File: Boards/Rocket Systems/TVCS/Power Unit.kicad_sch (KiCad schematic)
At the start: 111 parts, among them IC3 CYPD3177-24LQXQT, IC8 DMP2040USD-13, IC9 DMP2040USD-13, J10 DX07S016JA1R1500, U13 LM61460AASQRJRRQ1, U14 LM61460AASQRJRRQ1, U4 LM61460AASQRJRRQ1

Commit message: TVCS fixes and required additions
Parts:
- added TP1, TP2, TP3: TestPoint, TestPoint:TestPoint_Pad_2.0x2.0mm, symbol Connector:TestPoint
- Rsense3: value 7.5m -> 20m
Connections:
- net DC.DC1 PGOOD: now also TP1.1
- net DC.DC2 PGOOD: now also C_BIAS1.2, TP2.1
- net DC.DC3 PGOOD: now also C_BIAS2.2, TP3.1
- net GND: no longer C_BIAS1.2, C_BIAS2.2
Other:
- note added: "FALTA AQUI O POWER SWITCH USB-C LED Driver"
- note removed: "FALTA AQUI O POWER SWITCH USB-C LED Driver PGOOD LEDs"
- moved on the sheet: C10, C16, C17, C18, C19, C22, C24, C25, C28, C29, C30, C_BIAS1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

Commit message: Gnd update
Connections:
- net GND: no longer C10.2, C16.2, C17.2, C18.2, C19.2, C22.2, C24.2, C25.2, C28.2, C29.2, C30.2, C_IN-BLK1.2, C_IN-BLK2.2, C_IN-BLK3.2, C_IN1.2, C_IN2.2, C_IN3.2, C_IN4.2, C_IN5.2, C_IN6.2, C_IN_HFI1.2, C_IN_HFI2.2, C_IN_HFI3.2, C_IN_HFI4.2, C_IN_HFI5.2, C_IN_HFI6.2, C_OUT1.2, C_OUT10.2, C_OUT11.2, C_OUT12.2, C_OUT13.2, C_OUT14.2, C_OUT15.2, C_OUT16.2, C_OUT2.2, C_OUT3.2, C_OUT4.2, C_OUT5.2, C_OUT6.2, C_OUT7.2, C_OUT8.2, C_OUT9.2, C_VCC1.2, C_VCC2.2, C_VCC3.2, D3.2 (GND), IC3.19 (GND), IC3.22 (VSS), IC3.25 (EP), J10.1 (GND), J10.12 (GND), R_FBB1.1, R_FBB3.1, R_FBB5.1, R_RT1.1, R_RT2.1, R_RT3.1, U13.11 (PGND2), U13.3 (AGND), U13.9 (PGND1), U14.11 (PGND2), U14.3 (AGND), U14.9 (PGND1), U4.11 (PGND2), U4.3 (AGND), U4.9 (PGND1)
- new net GNDA: C16.2, C17.2, C18.2, C19.2, C22.2, C_IN-BLK1.2, C_IN-BLK2.2, C_IN-BLK3.2, C_IN1.2, C_IN2.2, C_IN3.2, C_IN4.2, C_IN5.2, C_IN6.2, C_IN_HFI1.2, C_IN_HFI2.2, C_IN_HFI3.2, C_IN_HFI4.2, C_IN_HFI5.2, C_IN_HFI6.2, C_OUT1.2, C_OUT10.2, C_OUT11.2, C_OUT12.2, C_OUT13.2, C_OUT14.2, C_OUT15.2, C_OUT16.2, C_OUT2.2, C_OUT3.2, C_OUT4.2, C_OUT5.2, C_OUT6.2, C_OUT7.2, C_OUT8.2, C_OUT9.2, C_VCC1.2, C_VCC2.2, C_VCC3.2, D3.2 (GND), IC3.19 (GND), IC3.22 (VSS), IC3.25 (EP), J10.1 (GND), J10.12 (GND), R_FBB1.1, R_FBB3.1, R_FBB5.1, R_RT1.1, R_RT2.1, R_RT3.1, U13.11 (PGND2), U13.3 (AGND), U13.9 (PGND1), U14.11 (PGND2), U14.3 (AGND), U14.9 (PGND1), U4.11 (PGND2), U4.3 (AGND), U4.9 (PGND1)
- new net GNDPWR: C10.2, C24.2, C25.2, C28.2, C29.2, C30.2

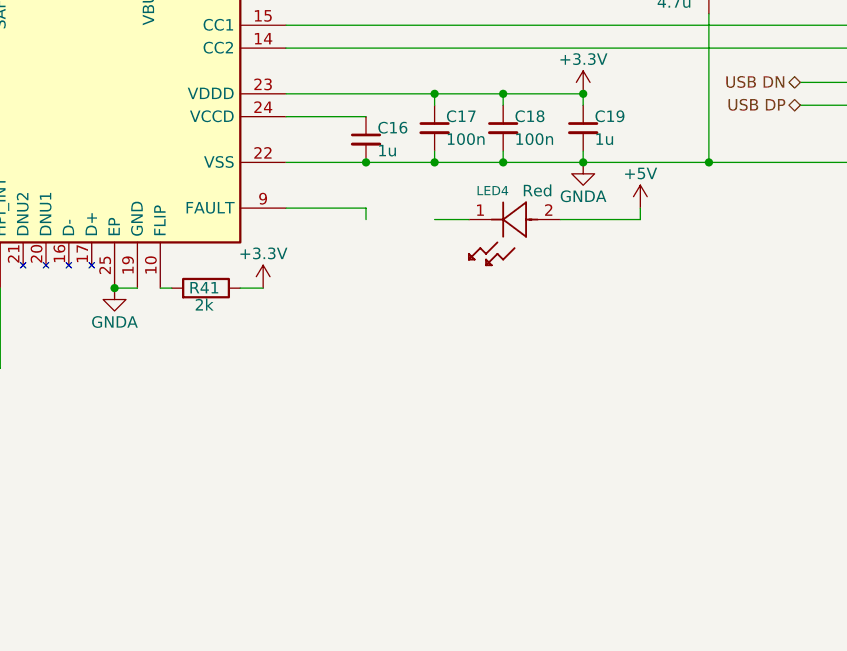
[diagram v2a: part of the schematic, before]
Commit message: added a driver for the led in the adc
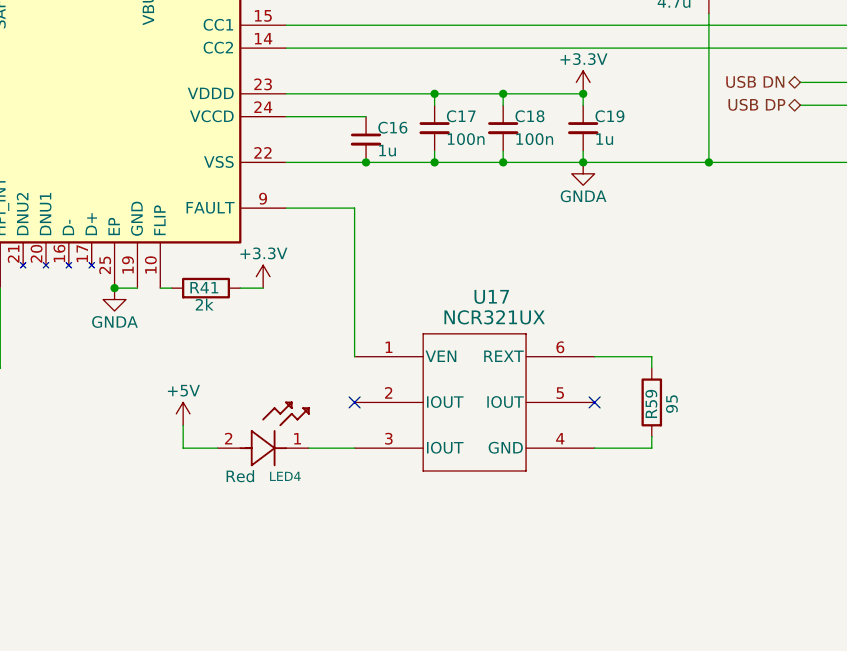
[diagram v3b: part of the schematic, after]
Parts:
- added R59: 95, Resistor-0402:RES_0402, symbol Device:R
- added U17: NCR321UX, TSOP6_SOT457_NEX, symbol NCR321UX:NCR321UX
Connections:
- net at IC3.9 (FAULT): now also U17.1 (VEN)
- net at LED4.1: now also U17.3 (IOUT)
- new net: R59.1, U17.6 (REXT)
- new net: R59.2, U17.4 (GND)
- no-connect marks 3 -> 5
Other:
- moved on the sheet: LED4
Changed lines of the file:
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@@
 		(at 439.42 91.44)
 	)
+	(no_connect
+		(at 368.3 128.27)
+	)
+	(no_connect
+		(at 341.63 128.27)
+	)
 	(wire
 		(pts
@@
 	(wire
 		(pts
-			(xy 184.15 96.52) (xy 194.31 96.52)
+			(xy 334.01 106.68) (xy 341.63 106.68)
 		)
 		(stroke
@@
 	(wire
 		(pts
-			(xy 302.26 58.42) (xy 302.26 60.96)
+			(xy 184.15 96.52) (xy 194.31 96.52)
 		)
 		(stroke
@@
 	(wire
 		(pts
-			(xy 116.84 269.24) (xy 116.84 276.86)
+			(xy 302.26 58.42) (xy 302.26 60.96)
 		)
 		(stroke
@@
 	(wire
 		(pts
-			(xy 107.95 140.97) (xy 121.92 140.97)
+			(xy 116.84 269.24) (xy 116.84 276.86)
 		)
 		(stroke
@@
 	(wire
 		(pts
-			(xy 111.76 185.42) (xy 111.76 195.58)
+			(xy 107.95 140.97) (xy 121.92 140.97)
 		)
 		(stroke
@@
 	(wire
 		(pts
-			(xy 373.38 106.68) (xy 373.38 107.95)
+			(xy 111.76 185.42) (xy 111.76 195.58)
 		)
 		(stroke
@@
 	(wire
 		(pts
+			(xy 322.58 133.35) (xy 326.39 133.35)
+		)
+		(stroke
+			(width 0)
+			(type default)
+		)
+	)
+	(wire
+		(pts
 			(xy 40.64 88.9) (xy 40.64 81.28)
 		)
@@
 	(wire
 		(pts
+			(xy 322.58 130.81) (xy 322.58 133.35)
+		)
+		(stroke
+			(width 0)
+			(type default)
+		)
+	)
+	(wire
+		(pts
 			(xy 107.95 146.05) (xy 107.95 147.32)
 		)
@@
 	(wire
 		(pts
-			(xy 342.9 106.68) (xy 334.01 106.68)
+			(xy 323.85 269.24) (xy 323.85 270.51)
 		)
 		(stroke
@@
 	(wire
 		(pts
-			(xy 323.85 269.24) (xy 323.85 270.51)
+			(xy 40.64 180.34) (xy 40.64 172.72)
 		)
 		(stroke
@@
 	(wire
 		(pts
-			(xy 40.64 180.34) (xy 40.64 172.72)
+			(xy 400.05 95.25) (xy 408.94 95.25)
 		)
 		(stroke
@@
 	(wire
 		(pts
-			(xy 400.05 95.25) (xy 408.94 95.25)
+			(xy 374.65 133.35) (xy 374.65 132.08)
 		)
 		(stroke
@@
 	(wire
 		(pts
-			(xy 342.9 106.68) (xy 342.9 107.95)
+			(xy 114.3 259.08) (xy 114.3 257.81)
 		)
 		(stroke
@@
 	(wire
 		(pts
-			(xy 114.3 259.08) (xy 114.3 257.81)
+			(xy 336.55 133.35) (xy 341.63 133.35)
 		)
 		(stroke
@@
 	(wire
 		(pts
+			(xy 368.3 123.19) (xy 374.65 123.19)
+		)
+		(stroke
+			(width 0)
+			(type default)
+		)
+	)
+	(wire
+		(pts
 			(xy 257.81 269.24) (xy 283.21 269.24)
 		)
@@
 	(wire
 		(pts
+			(xy 374.65 123.19) (xy 374.65 124.46)
+		)
+		(stroke
+			(width 0)
+			(type default)
+		)
+	)
+	(wire
+		(pts
 			(xy 142.24 173.99) (xy 151.13 173.99)
 		)
@@
 	(wire
 		(pts
+			(xy 341.63 106.68) (xy 341.63 123.19)
+		)
+		(stroke
+			(width 0)
+			(type default)
+		)
+	)
+	(wire
+		(pts
 			(xy 205.74 257.81) (xy 205.74 284.48)
 		)
@@
 	(wire
 		(pts
+			(xy 368.3 133.35) (xy 374.65 133.35)
+		)
+		(stroke
+			(width 0)
+			(type default)
+		)
+	)
+	(wire
+		(pts
 			(xy 149.86 153.67) (xy 179.07 153.67)
 		)
@@
 	(wire
 		(pts
-			(xy 364.49 107.95) (xy 373.38 107.95)
-		)
-		(stroke
-			(width 0)
-			(type default)
-		)
-	)
-	(wire
-		(pts
 			(xy 367.03 93.98) (xy 367.03 95.25)
 		)
@@
 	(wire
 		(pts
-			(xy 350.52 107.95) (xy 354.33 107.95)
-		)
-		(stroke
-			(width 0)
-			(type default)
-		)
-	)
-	(wire
-		(pts
 			(xy 153.67 265.43) (xy 163.83 265.43)
 		)
@@
 	(symbol
 		(lib_id "VLMS1500-GS08:VLMS1500-GS08")
-		(at 364.49 107.95 180)
+		(at 326.39 133.35 0)
 		(unit 1)
 		(exclude_from_sim no)
@@
 		(dnp no)
 		(property "Reference" "LED4"
-			(at 358.775 104.775 0)
+			(at 332.105 136.525 0)
 			(effects
 				(font
@@
 		)
 		(property "Value" "VLMS1500-GS08"
-			(at 356.8701 114.3 90)
+			(at 334.0099 127 90)
 			(effects
 				(font
@@
 		)
 		(property "Footprint" "LED-Red_VLMS1500-GS08:LED_00-GS08_VIS_RED"
-			(at 364.49 107.95 0)
+			(at 326.39 133.35 0)
 			(effects
 				(font
@@
 		)
 		(property "Datasheet" "VLMS1500-GS08"
-			(at 364.49 107.95 0)
+			(at 326.39 133.35 0)
 			(effects
 				(font
@@
 		)
 		(property "Description" "Red"
-			(at 361.95 104.775 0)
+			(at 328.93 136.525 0)
 			(effects
 				(font
@@
 	)
 	(symbol
+		(lib_id "Device:R")
+		(at 374.65 128.27 0)
+		(mirror y)
+		(unit 1)
+		(exclude_from_sim no)
+		(in_bom yes)
+		(on_board yes)
+		(dnp no)
+		(property "Reference" "R59"
+			(at 374.65 130.175 90)
+			(effects
+				(font
+					(size 1.27 1.27)
+				)
+				(justify left)
+			)
+		)
+		(property "Value" "95"
+			(at 376.936 129.54 90)
+			(effects
+				(font
+					(size 1.27 1.27)
+				)
+				(justify left)
+			)
+		)
+		(property "Footprint" "Resistor-0402:RES_0402"
+			(at 376.428 128.27 90)
+			(effects
+				(font
+					(size 1.27 1.27)
+				)
+				(hide yes)
+			)
+		)
+		(property "Datasheet" "~"
+			(at 374.65 128.27 0)
+			(effects
+				(font
+					(size 1.27 1.27)
+				)
+				(hide yes)
+			)
+		)
+		(property "Description" "Resistor"
+			(at 374.65 128.27 0)
+			(effects
+				(font
+					(size 1.27 1.27)
+				)
+				(hide yes)
+			)
+		)
+		(pin "1"
+		)
+		(pin "2"
+		)
+		(instances
+			(project "TVCS"
+				(path "/2cb205da-01dc-4dd5-90f3-3844dc2f7334/1d3e1938-2181-482b-a6e3-3e03c94a0c3c"
+					(reference "R59")
+					(unit 1)
+				)
+			)
+		)
+	)
+	(symbol
 		(lib_id "Device:L")
 		(at 120.65 74.93 90)
@@
 	)
 	(symbol
+		(lib_id "NCR321UX:NCR321UX")
+		(at 341.63 125.73 0)
+		(unit 1)
+		(exclude_from_sim no)
+		(in_bom yes)
+		(on_board yes)
+		(dnp no)
+		(fields_autoplaced yes)
+		(property "Reference" "U17"
+			(at 356.87 116.586 0)
+			(effects
+				(font
+					(size 1.524 1.524)
+				)
+			)
+		)
+		(property "Value" "NCR321UX"
+			(at 357.124 118.872 0)
+			(effects
+				(font
+					(size 1.524 1.524)
+				)
+			)
+		)
+		(property "Footprint" "TSOP6_SOT457_NEX"
+			(at 341.63 125.73 0)
+			(effects
+				(font
+					(size 1.27 1.27)
+					(italic yes)
+				)
+				(hide yes)
+			)
+		)
+		(property "Datasheet" "NCR321UX"
+			(at 341.63 125.73 0)
+			(effects
+				(font
+					(size 1.27 1.27)
+					(italic yes)
+				)
+				(hide yes)
+			)
+		)
+		(property "Description" ""
+			(at 341.63 125.73 0)
+			(effects
+				(font
+					(size 1.27 1.27)
+				)
+				(hide yes)
+			)
+		)
+		(pin "4"
+		)
+		(pin "1"
+		)
+		(pin "3"
+		)
+		(pin "6"
+		)
+		(pin "5"
+		)
+		(pin "2"
+		)
+		(instances
+			(project ""
+				(path "/2cb205da-01dc-4dd5-90f3-3844dc2f7334/1d3e1938-2181-482b-a6e3-3e03c94a0c3c"
+					(reference "U17")
+					(unit 1)
+				)
+			)
+		)
+	)
+	(symbol
 		(lib_id "Device:R")
 		(at 40.64 184.15 0)
@@
 	(symbol
 		(lib_id "power:+5V")
-		(at 373.38 106.68 0)
+		(at 322.58 130.81 0)
 		(unit 1)
 		(exclude_from_sim no)
@@
 		(dnp no)
 		(property "Reference" "#PWR0123"
-			(at 373.38 110.49 0)
+			(at 322.58 134.62 0)
 			(effects
 				(font
@@
 		)
 		(property "Value" "+5V"
-			(at 373.38 102.87 0)
+			(at 322.58 127 0)
 			(effects
 				(font
@@
 		)
 		(property "Footprint" ""
-			(at 373.38 106.68 0)
+			(at 322.58 130.81 0)
 			(effects
 				(font
@@
 		)
 		(property "Datasheet" ""
-			(at 373.38 106.68 0)
+			(at 322.58 130.81 0)
 			(effects
 				(font
@@
 		)
 		(property "Description" "Power symbol creates a global label with name \"+5V\""
-			(at 373.38 106.68 0)
+			(at 322.58 130.81 0)
 			(effects
 				(font
